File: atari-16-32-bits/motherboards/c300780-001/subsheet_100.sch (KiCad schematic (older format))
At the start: 1 part, among them U100 MC68000_PLCC_68_PHY

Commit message: done u100,u101
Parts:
- added C111, C112: 0.1uF, symbol Device:C
- added P100: 1K2 ×8, Resistor_THT:R_Array_SIP9, symbol Device:R_Network08_US
- added P101, P102, P103: 4K7 ×8, Resistor_THT:R_Array_SIP9, symbol Device:R_Network08_US
- added P104, P105: 10K ×8, Resistor_THT:R_Array_SIP9, symbol Device:R_Network08_US
- added R102, R107: 1K, symbol Device:R_US
- added R103, R104, R105: 10K, symbol Device:R_US
- added R109: 2K2, symbol Device:R_US
- added R110: 4K7, symbol Device:R_US
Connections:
- net D0: now also P105.2 (R1)
- net D1: now also P105.3 (R2)
- net D10: now also P104.4 (R3)
- net D11: now also P104.5 (R4)
- net D12: now also P104.6 (R5)
- net D13: now also P104.7 (R6)
- net D14: now also P104.8 (R7)
- net D15: now also P104.9 (R8)
- net D2: now also P105.4 (R3)
- net D3: now also P105.5 (R4)
- net D4: now also P105.6 (R5)
- net D5: now also P105.7 (R6)
- net D6: now also P105.8 (R7)
- net D7: now also P105.9 (R8)
- net D8: now also P104.2 (R1)
- net D9: now also P104.3 (R2)
- net GND: now also C111.2, C112.2
- net VCC: now also C111.1, C112.1, P100.1 (common), P101.1 (common), P102.1 (common), P103.1 (common), P104.1 (common), P105.1 (common), R102.1, R103.1, R104.1, R105.1, R107.1, R109.1, R110.1
- net XDTACK: now reaches U100.10 (~DTACK~)
- net XDTACK: now also R102.2
- net XCPUBG: now reaches U100.11 (~BG~)
- net XBGACK: now reaches U100.12 (~BGACK~)
- net XBGACK: now also P100.4 (R3)
- net XBR: now reaches U100.13 (~BR~)
- net XBR: now also P100.5 (R4)
- net CLK8: now reaches U100.15 (CLK)
- net XHALT: now reaches U100.19 (~HALT~)
- net XHALT: now also P100.2 (R1)
- net XRESET: now reaches U100.20 (~RESET~)
- net XRESET: now also R107.2
- net XVMA: now reaches U100.21 (~VMA~)
- net XVMA: now also R110.2
- net E: now reaches U100.22 (E)
- net XVPA: now reaches U100.23 (~VPA~)
- net XVPA: now also R109.2
- net XBERR: now reaches U100.24 (~BERR~)
- net XBERR: now also P100.3 (R2)
- net IPL2: now reaches U100.25 (IPL2)
- net IPL1: now reaches U100.26 (IPL1)
- net IPL0: now reaches U100.27 (IPL0)
- net FC2: now reaches U100.28 (FC2)
- net FC2: now also R103.2
- net FC1: now reaches U100.29 (FC1)
- net FC1: now also R104.2
- net FC0: now reaches U100.30 (FC0)
- net FC0: now also R105.2
- net A1: now reaches U100.32 (A1)
- net A1: now also P103.2 (R1)
- net A2: now reaches U100.33 (A2)
- net A2: now also P103.3 (R2)
- net A3: now reaches U100.34 (A3)
- net A3: now also P103.4 (R3)
- net A4: now reaches U100.35 (A4)
- net A4: now also P103.5 (R4)
- net A5: now reaches U100.36 (A5)
- net A5: now also P103.6 (R5)
- net A6: now reaches U100.37 (A6)
- net A6: now also P103.7 (R6)
- net A7: now reaches U100.38 (A7)
- net A7: now also P103.8 (R7)
- net A8: now reaches U100.39 (A8)
- net A8: now also P103.9 (R8)
- net A9: now reaches U100.40 (A9)
- net A9: now also P102.2 (R1)
- net A10: now reaches U100.41 (A10)
- net A10: now also P102.3 (R2)
- net A11: now reaches U100.42 (A11)
- net A11: now also P102.4 (R3)
- net A12: now reaches U100.43 (A12)
- net A12: now also P102.5 (R4)
- net A13: now reaches U100.44 (A13)
- net A13: now also P102.6 (R5)
- net A14: now reaches U100.45 (A14)
- net A14: now also P102.7 (R6)
- net A15: now reaches U100.46 (A15)
- net A15: now also P102.8 (R7)
- net A16: now reaches U100.47 (A16)
- net A16: now also P102.9 (R8)
- net A17: now reaches U100.48 (A17)
- net A17: now also P101.9 (R8)
- net A18: now reaches U100.49 (A18)
- net A18: now also P101.8 (R7)
- net A19: now reaches U100.50 (A19)
- net A19: now also P101.7 (R6)
- net A20: now reaches U100.51 (A20)
- net A20: now also P101.6 (R5)
- net A21: now reaches U100.53 (A21)
- net A21: now also P101.5 (R4)
- net A22: now reaches U100.54 (A22)
- net A22: now also P101.4 (R3)
- net A23: now reaches U100.55 (A23)
- net A23: now also P101.3 (R2)
- net XAS: now reaches U100.6 (~AS~)
- net XAS: now also P100.9 (R8)
- net XUDS: now reaches U100.7 (~UDS~)
- net XUDS: now also P100.8 (R7)
- net XLDS: now reaches U100.8 (~LDS~)
- net XLDS: now also P100.7 (R6)
- net RXW: now reaches U100.9 (R/~W~)
- net RXW: now also P100.6 (R5)
- no-connect marks 0 -> 1
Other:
- moved on the sheet: U100

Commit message: sheet 1 done
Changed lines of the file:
@@
 Text GLabel 1850 3500 0    50   Output ~ 0
 XVMA
-Text GLabel 1850 3400 0    50   Output ~ 0
+Text GLabel 1850 3400 0    50   BiDi ~ 0
 XRESET
 Text GLabel 1850 3300 0    50   Output ~ 0

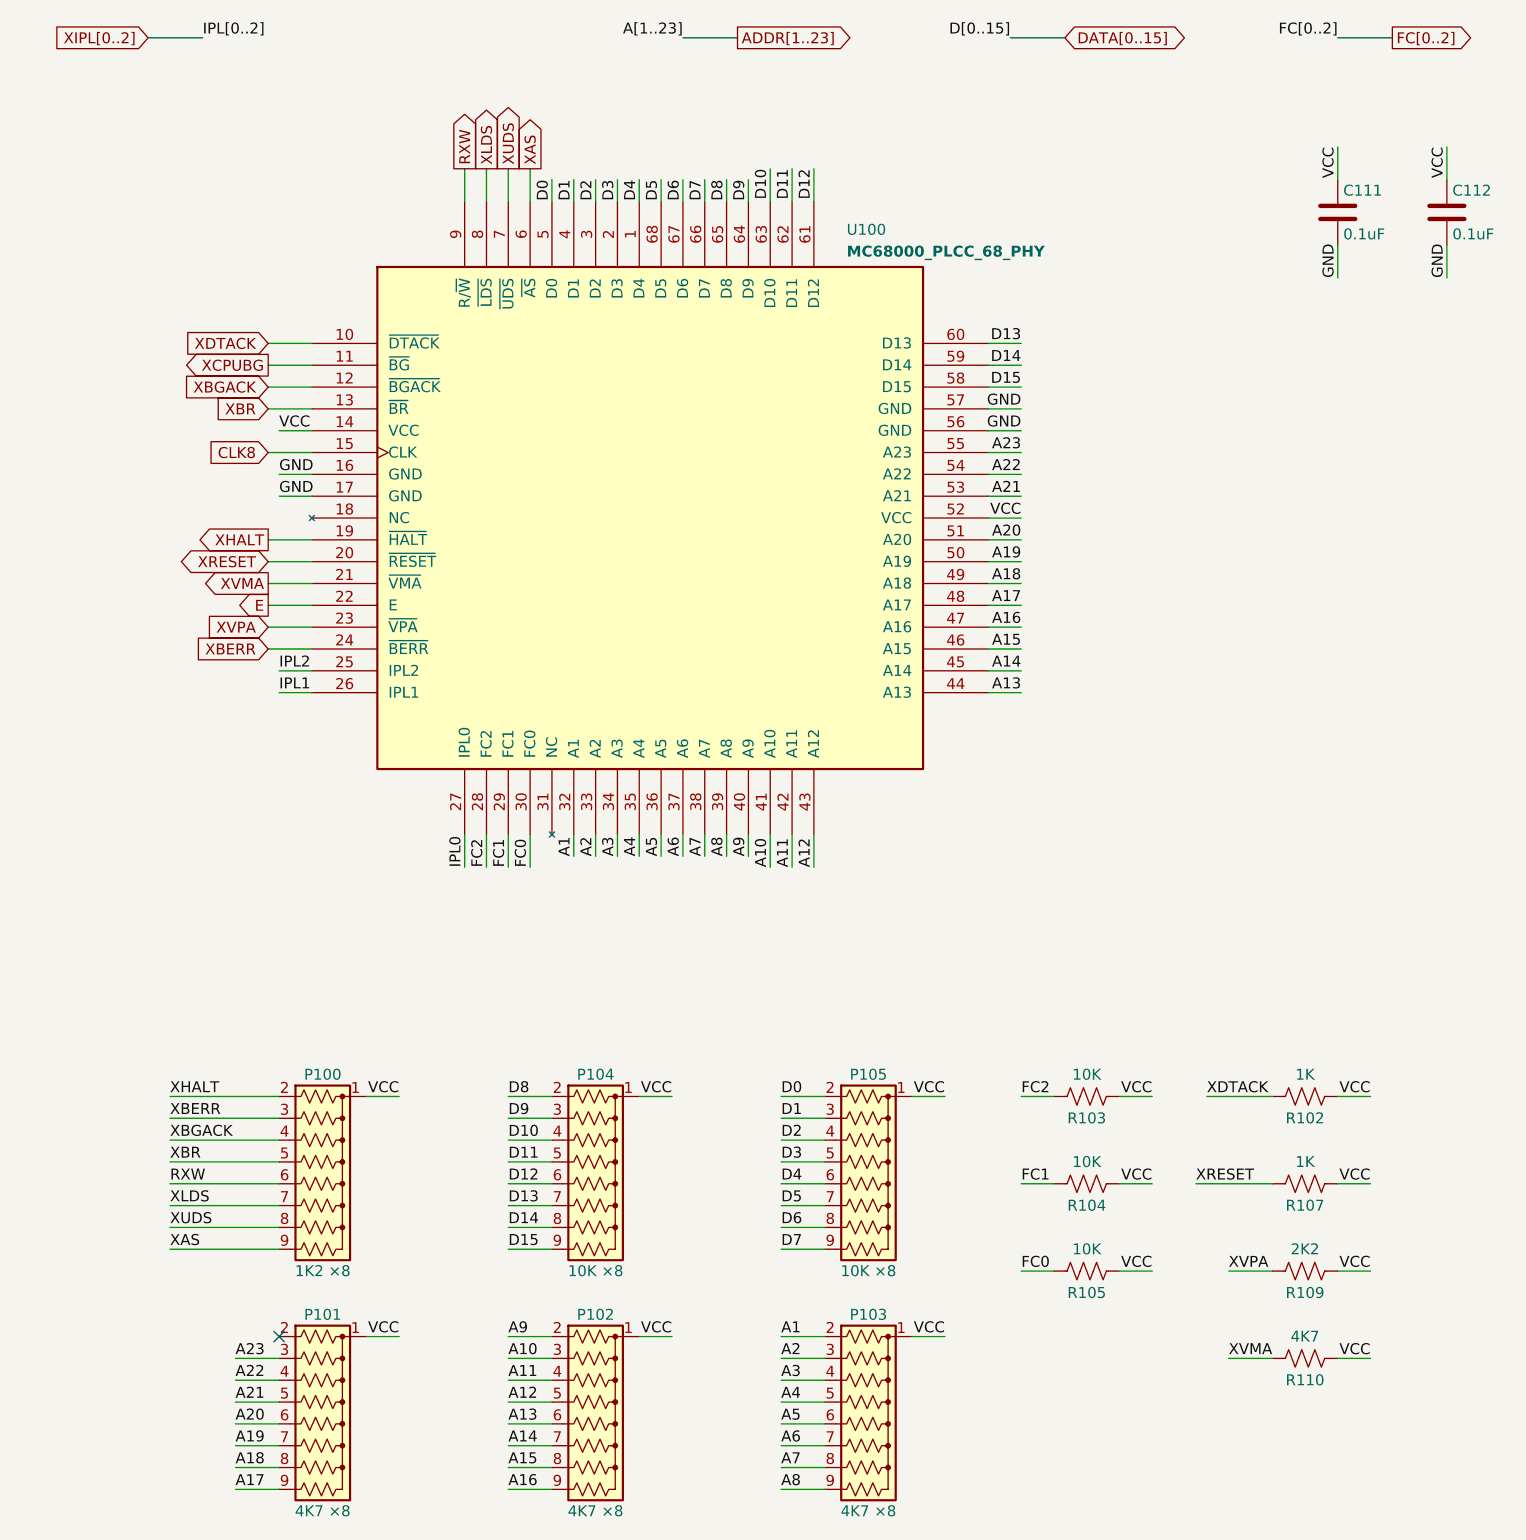
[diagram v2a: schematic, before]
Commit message: reorganized sheets
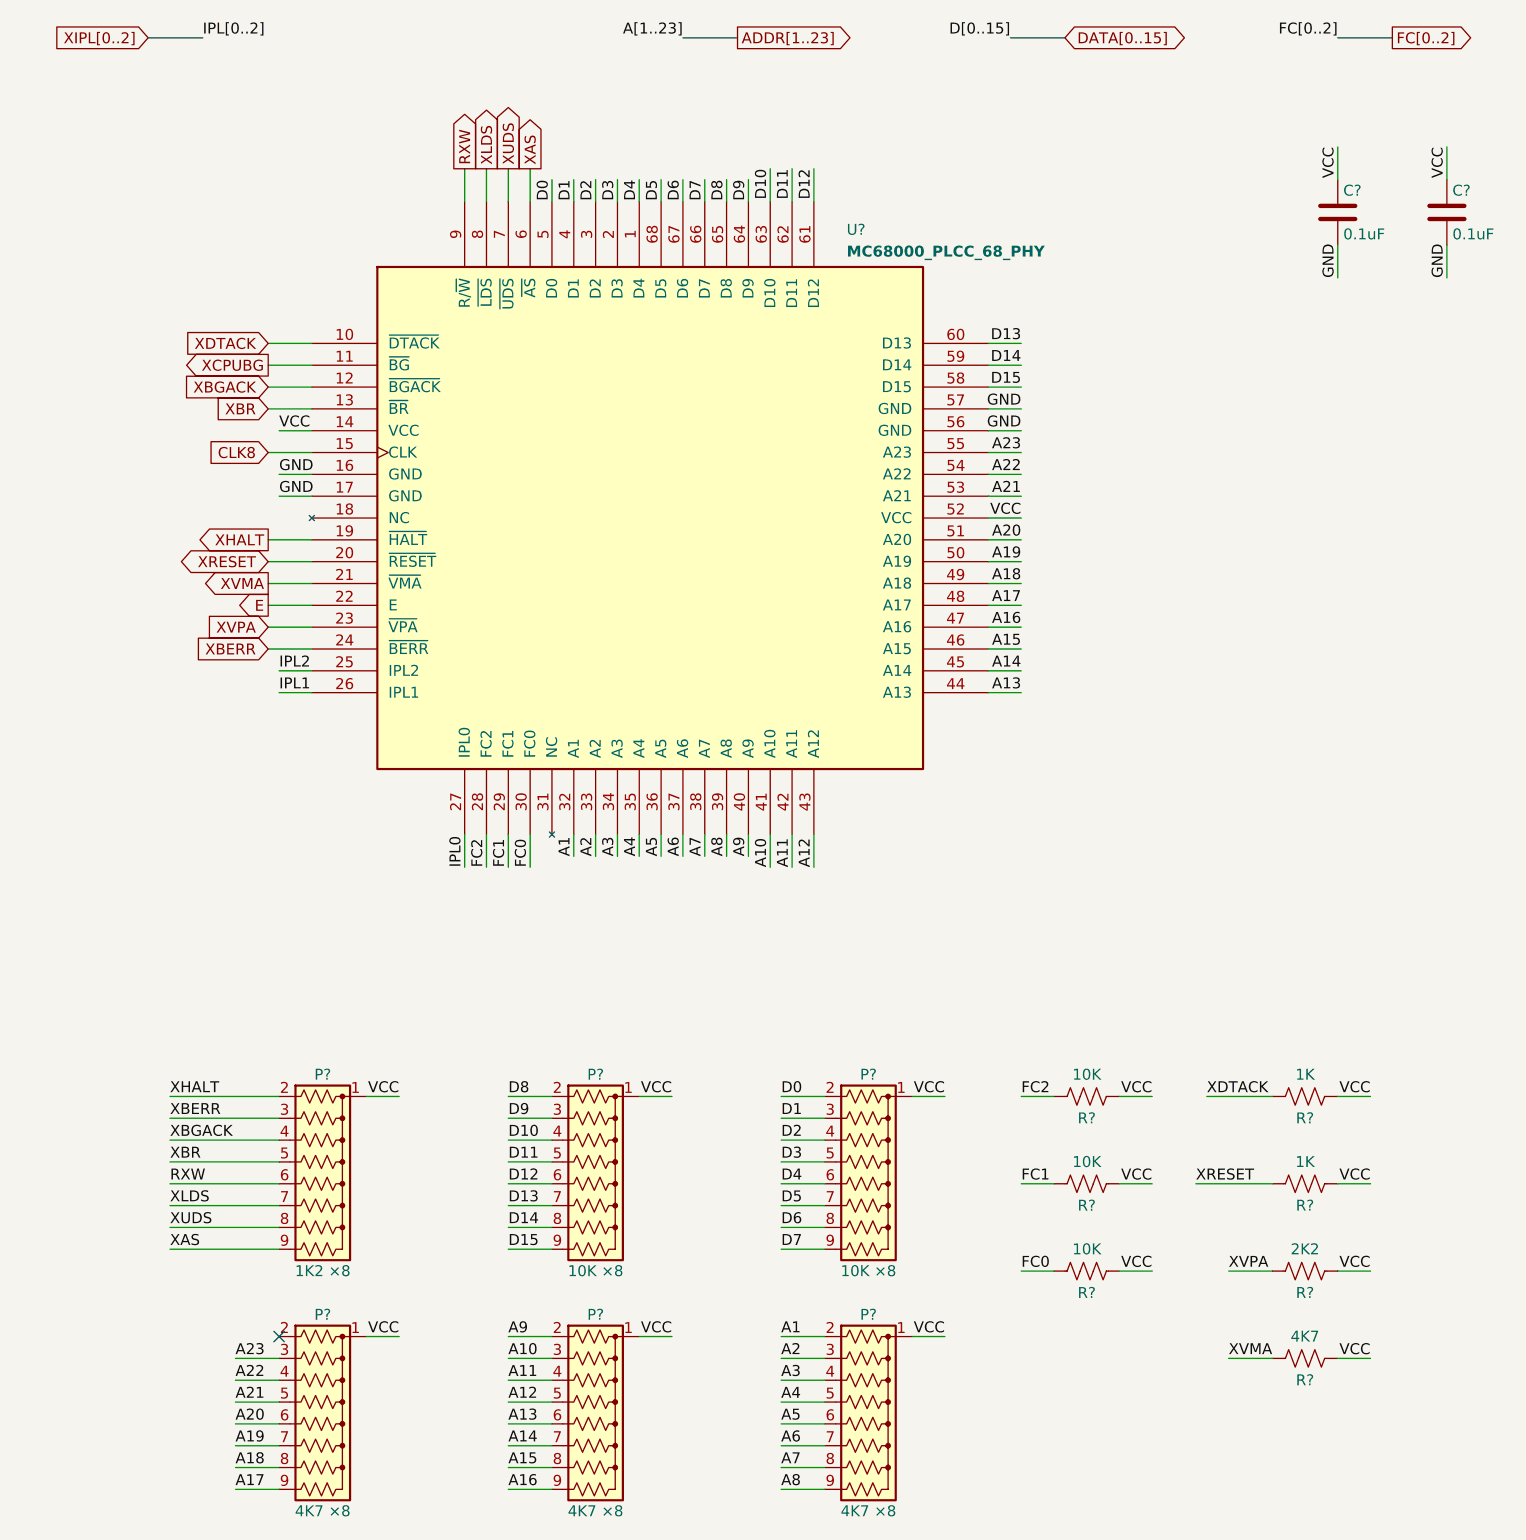
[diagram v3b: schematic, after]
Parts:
- renumbered P100 to P?, P101 to P?, P102 to P?, P103 to P?, P104 to P?, P105 to P?, R102 to R?, R103 to R?, R104 to R?, R105 to R?, R107 to R?, R109 to R?, R110 to R?, U100 to U?
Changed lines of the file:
@@
 $Descr A4 8268 11693 portrait
 encoding utf-8
-Sheet 3 14
+Sheet 14 8
 Title ""
 Date ""
@@
 GND
 $Comp
-L mc_68000_plcc68:MC68000_PLCC_68_PHY U100
+L mc_68000_plcc68:MC68000_PLCC_68_PHY U?
 U 1 1 607B5358
 P 3600 3200
-F 0 "U100" H 4500 4550 50  0000 L TNN
+F 0 "U?" H 4500 4550 50  0000 L TNN
 F 1 "MC68000_PLCC_68_PHY" H 4500 4450 50  0000 L TNB
 F 2 "Package_LCC:PLCC-68_THT-Socket" H 4500 4650 50  0001 L TNN
@@
 AR Path="/60786F27/6078774E/607ECFCE" Ref="C?"  Part="1"
 AR Path="/60786F27/607874AD/607ECFCE" Ref="C111"  Part="1"
-F 0 "C111" H 6775 1900 50  0000 L CNN
+AR Path="/6089D0C6/607ECFCE" Ref="C?"  Part="1"
+F 0 "C?" H 6775 1900 50  0000 L CNN
 F 1 "0.1uF" H 6775 1700 50  0000 L CNN
 F 2 "" H 6788 1650 50  0001 C CNN
@@
 AR Path="/60786F27/6078774E/607ECFD4" Ref="C?"  Part="1"
 AR Path="/60786F27/607874AD/607ECFD4" Ref="C112"  Part="1"
-F 0 "C112" H 7275 1900 50  0000 L CNN
+AR Path="/6089D0C6/607ECFD4" Ref="C?"  Part="1"
+F 0 "C?" H 7275 1900 50  0000 L CNN
 F 1 "0.1uF" H 7275 1700 50  0000 L CNN
 F 2 "" H 7288 1650 50  0001 C CNN
@@
 	7250 1500 7250 1650
 $Comp
-L Device:R_Network08_US P100
+L Device:R_Network08_US P?
 U 1 1 607F5888
 P 2100 6250
-F 0 "P100" V 1600 6250 50  0000 C CNN
+F 0 "P?" V 1600 6250 50  0000 C CNN
 F 1 "1K2 ×8" V 2500 6250 50  0000 C CNN
 F 2 "Resistor_THT:R_Array_SIP9" V 2575 6250 50  0001 C CNN
@@
 $EndComp
 $Comp
-L Device:R_Network08_US P101
+L Device:R_Network08_US P?
 U 1 1 607F7061
 P 2100 7350
-F 0 "P101" V 1600 7350 50  0000 C CNN
+F 0 "P?" V 1600 7350 50  0000 C CNN
 F 1 "4K7 ×8" V 2500 7350 50  0000 C CNN
 F 2 "Resistor_THT:R_Array_SIP9" V 2575 7350 50  0001 C CNN
@@
 $EndComp
 $Comp
-L Device:R_Network08_US P102
+L Device:R_Network08_US P?
 U 1 1 607F8D98
 P 3350 7350
-F 0 "P102" V 2850 7350 50  0000 C CNN
+F 0 "P?" V 2850 7350 50  0000 C CNN
 F 1 "4K7 ×8" V 3750 7350 50  0000 C CNN
 F 2 "Resistor_THT:R_Array_SIP9" V 3825 7350 50  0001 C CNN
@@
 $EndComp
 $Comp
-L Device:R_Network08_US P103
+L Device:R_Network08_US P?
 U 1 1 607F991C
 P 4600 7350
-F 0 "P103" V 4100 7350 50  0000 C CNN
+F 0 "P?" V 4100 7350 50  0000 C CNN
 F 1 "4K7 ×8" V 5000 7350 50  0000 C CNN
 F 2 "Resistor_THT:R_Array_SIP9" V 5075 7350 50  0001 C CNN
@@
 $EndComp
 $Comp
-L Device:R_Network08_US P104
+L Device:R_Network08_US P?
 U 1 1 607FB176
 P 3350 6250
-F 0 "P104" V 2850 6250 50  0000 C CNN
+F 0 "P?" V 2850 6250 50  0000 C CNN
 F 1 "10K ×8" V 3750 6250 50  0000 C CNN
 F 2 "Resistor_THT:R_Array_SIP9" V 3825 6250 50  0001 C CNN
@@
 $EndComp
 $Comp
-L Device:R_Network08_US P105
+L Device:R_Network08_US P?
 U 1 1 60815C70
 P 4600 6250
-F 0 "P105" V 4100 6250 50  0000 C CNN
+F 0 "P?" V 4100 6250 50  0000 C CNN
 F 1 "10K ×8" V 5000 6250 50  0000 C CNN
 F 2 "Resistor_THT:R_Array_SIP9" V 5075 6250 50  0001 C CNN
@@
 NoConn ~ 1900 6950
 $Comp
-L Device:R_US R102
+L Device:R_US R?
 U 1 1 60907E08
 P 6600 5850
-F 0 "R102" V 6700 5850 50  0000 C CNN
+F 0 "R?" V 6700 5850 50  0000 C CNN
 F 1 "1K" V 6500 5850 50  0000 C CNN
 F 2 "" V 6640 5840 50  0001 C CNN
@@
 $EndComp
 $Comp
-L Device:R_US R103
+L Device:R_US R?
 U 1 1 6090DB64
 P 5600 5850
-F 0 "R103" V 5700 5850 50  0000 C CNN
+F 0 "R?" V 5700 5850 50  0000 C CNN
 F 1 "10K" V 5500 5850 50  0000 C CNN
 F 2 "" V 5640 5840 50  0001 C CNN
@@
 $EndComp
 $Comp
-L Device:R_US R104
+L Device:R_US R?
 U 1 1 6090DFB5
 P 5600 6250
-F 0 "R104" V 5700 6250 50  0000 C CNN
+F 0 "R?" V 5700 6250 50  0000 C CNN
 F 1 "10K" V 5500 6250 50  0000 C CNN
 F 2 "" V 5640 6240 50  0001 C CNN
@@
 $EndComp
 $Comp
-L Device:R_US R105
+L Device:R_US R?
 U 1 1 6090EA19
 P 5600 6650
-F 0 "R105" V 5700 6650 50  0000 C CNN
+F 0 "R?" V 5700 6650 50  0000 C CNN
 F 1 "10K" V 5500 6650 50  0000 C CNN
 F 2 "" V 5640 6640 50  0001 C CNN
@@
 	5750 6650 5900 6650
 $Comp
-L Device:R_US R107
+L Device:R_US R?
 U 1 1 6093D9ED
 P 6600 6250
-F 0 "R107" V 6700 6250 50  0000 C CNN
+F 0 "R?" V 6700 6250 50  0000 C CNN
 F 1 "1K" V 6500 6250 50  0000 C CNN
 F 2 "" V 6640 6240 50  0001 C CNN
@@
 $EndComp
 $Comp
-L Device:R_US R109
+L Device:R_US R?
 U 1 1 6093E40C
 P 6600 6650
-F 0 "R109" V 6700 6650 50  0000 C CNN
+F 0 "R?" V 6700 6650 50  0000 C CNN
 F 1 "2K2" V 6500 6650 50  0000 C CNN
 F 2 "" V 6640 6640 50  0001 C CNN
@@
 $EndComp
 $Comp
-L Device:R_US R110
+L Device:R_US R?
 U 1 1 6093E522
 P 6600 7050
-F 0 "R110" V 6700 7050 50  0000 C CNN
+F 0 "R?" V 6700 7050 50  0000 C CNN
 F 1 "4K7" V 6500 7050 50  0000 C CNN
 F 2 "" V 6640 7040 50  0001 C CNN
